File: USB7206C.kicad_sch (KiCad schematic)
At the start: 38 parts, among them J1 USB_SPI_(Opt), SW1 RESET_HUB, U2 MIC803-29D4VM3-TR, U27 USB7206C/KDX, Y1 25MHz

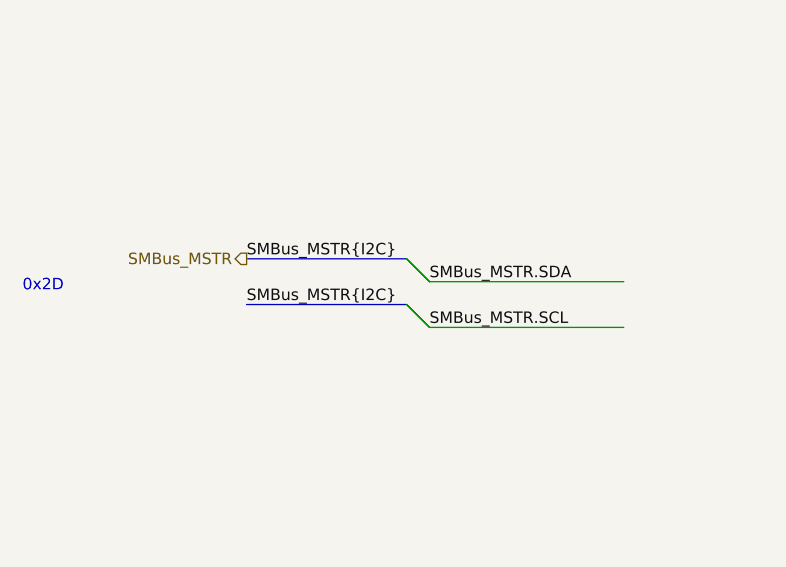
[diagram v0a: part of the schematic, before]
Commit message: Ferrite Breads added for 5V, TVS and ESD diodes added
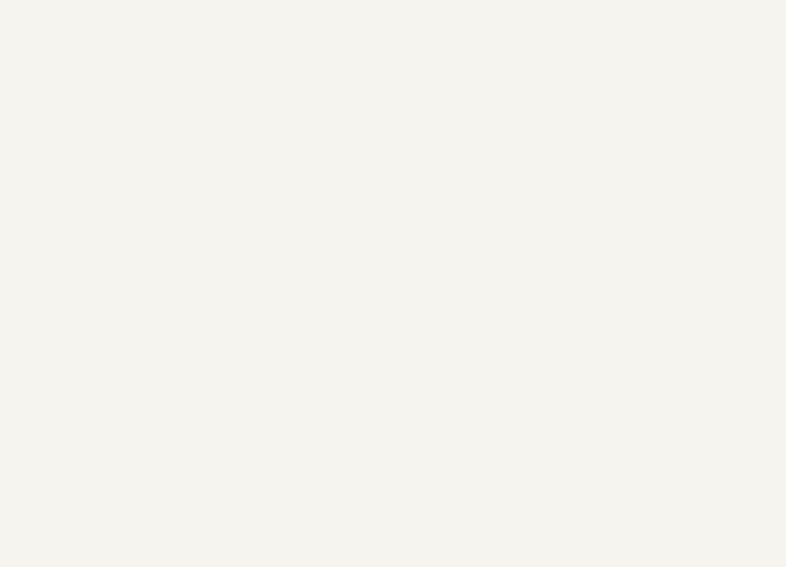
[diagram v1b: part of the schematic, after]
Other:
- note removed: "0x2D"
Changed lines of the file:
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@@
 		)
 	)
-	(text "0x2D"
-		(exclude_from_sim no)
-		(at -93.726 77.978 0)
-		(effects
-			(font
-				(size 1.27 1.27)
-			)
-		)
-	)
 	(text "VBUS Detection & ESD Protection"
 		(exclude_from_sim no)
@@
 	)
 	(bus_entry
-		(at -53.34 80.01)
-		(size 2.54 2.54)
-		(stroke
-			(width 0)
-			(type default)
-		)
-	)
-	(bus_entry
 		(at 191.77 26.67)
 		(size -2.54 2.54)
@@
 	)
 	(bus_entry
-		(at -53.34 74.93)
-		(size 2.54 2.54)
-		(stroke
-			(width 0)
-			(type default)
-		)
-	)
-	(bus_entry
 		(at 191.77 138.43)
 		(size -2.54 2.54)
@@
 	)
 	(bus_entry
-		(at -50.8 77.47)
-		(size -2.54 -2.54)
-		(stroke
-			(width 0)
-			(type default)
-		)
-	)
-	(bus_entry
 		(at 41.91 34.29)
 		(size 2.54 2.54)
@@
 	)
 	(bus_entry
-		(at -50.8 82.55)
-		(size -2.54 -2.54)
-		(stroke
-			(width 0)
-			(type default)
-		)
-	)
-	(bus_entry
 		(at 191.77 113.03)
 		(size -2.54 2.54)
@@
 	(wire
 		(pts
-			(xy -50.8 77.47) (xy -29.21 77.47)
-		)
-		(stroke
-			(width 0)
-			(type default)
-		)
-	)
-	(wire
-		(pts
 			(xy 44.45 41.91) (xy 60.96 41.91)
 		)
@@
 	(wire
 		(pts
-			(xy -50.8 82.55) (xy -29.21 82.55)
-		)
-		(stroke
-			(width 0)
-			(type default)
-		)
-	)
-	(wire
-		(pts
 			(xy 234.95 40.64) (xy 251.46 40.64)
 		)
@@
 		)
 	)
-	(bus
-		(pts
-			(xy -71.12 80.01) (xy -53.34 80.01)
-		)
-		(stroke
-			(width 0)
-			(type default)
-		)
-	)
 	(wire
 		(pts
@@
 		)
 	)
-	(bus
-		(pts
-			(xy -71.12 74.93) (xy -53.34 74.93)
-		)
-		(stroke
-			(width 0)
-			(type default)
-		)
-	)
 	(wire
 		(pts
@@
 		)
 	)
-	(label "SMBus_MSTR{I2C}"
-		(at -71.12 74.93 0)
-		(effects
-			(font
-				(size 1.27 1.27)
-			)
-			(justify left bottom)
-		)
-	)
 	(label "USB3_DN5.TX1-"
 		(at 172.72 137.16 0)
@@
 		)
 	)
-	(label "SMBus_MSTR.SDA"
-		(at -50.8 77.47 0)
-		(effects
-			(font
-				(size 1.27 1.27)
-			)
-			(justify left bottom)
-		)
-	)
 	(label "USB3_DN3.RX1+"
 		(at 172.72 90.17 0)
@@
 		)
 	)
-	(label "SMBus_MSTR.SCL"
-		(at -50.8 82.55 0)
-		(effects
-			(font
-				(size 1.27 1.27)
-			)
-			(justify left bottom)
-		)
-	)
 	(label "CFG_STRAP1"
 		(at 30.48 259.08 0)
@@
 		)
 	)
-	(label "SMBus_MSTR{I2C}"
-		(at -71.12 80.01 0)
-		(effects
-			(font
-				(size 1.27 1.27)
-			)
-			(justify left bottom)
-		)
-	)
 	(label "USB3_UP.RX1+"
 		(at 60.96 41.91 180)
@@
 		)
 	)
-	(hierarchical_label "SMBus_MSTR"
-		(shape output)
-		(at -71.12 74.93 180)
-		(effects
-			(font
-				(size 1.27 1.27)
-			)
-			(justify right)
-		)
-	)

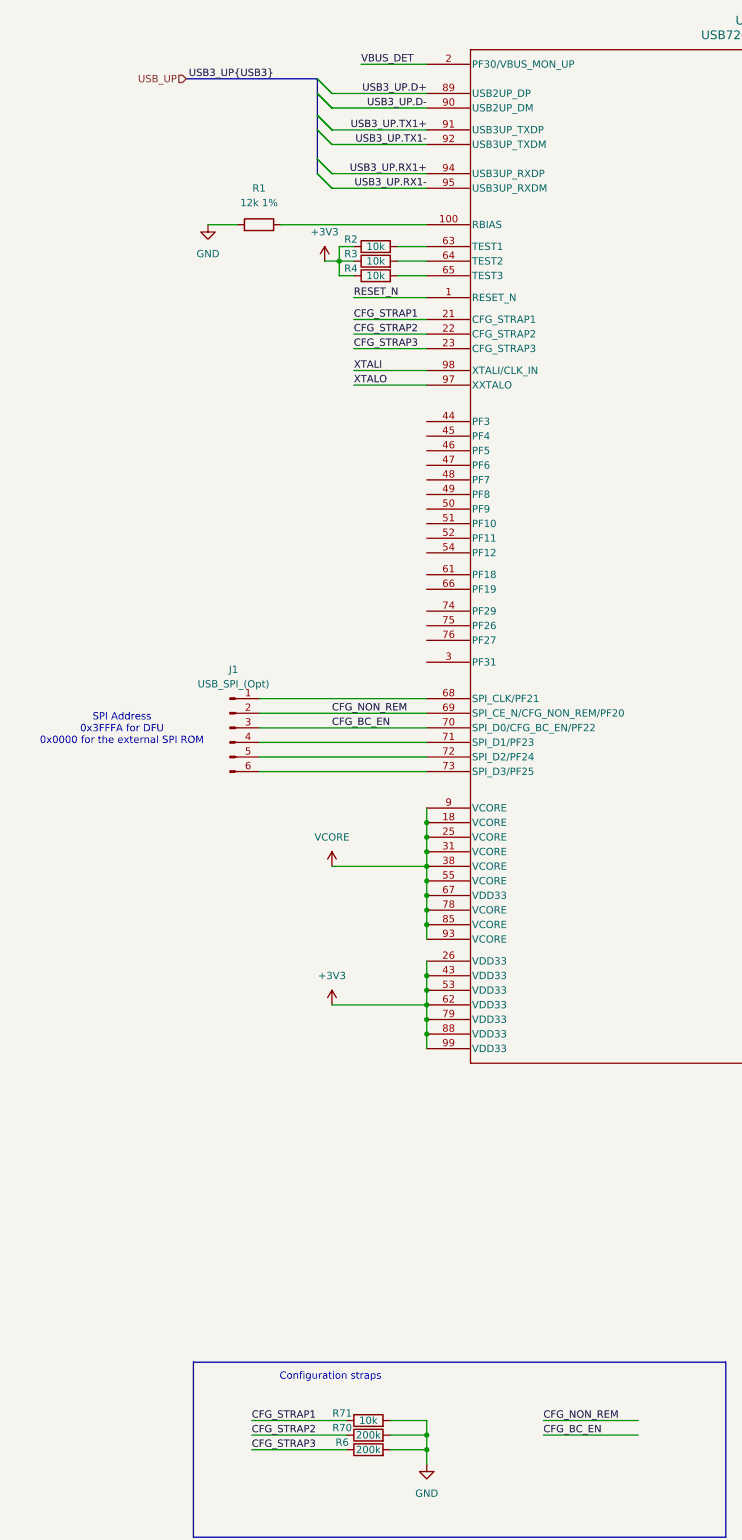
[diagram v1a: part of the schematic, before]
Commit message: Ferrite bread filter for LDO and MIC23201, labelling improved
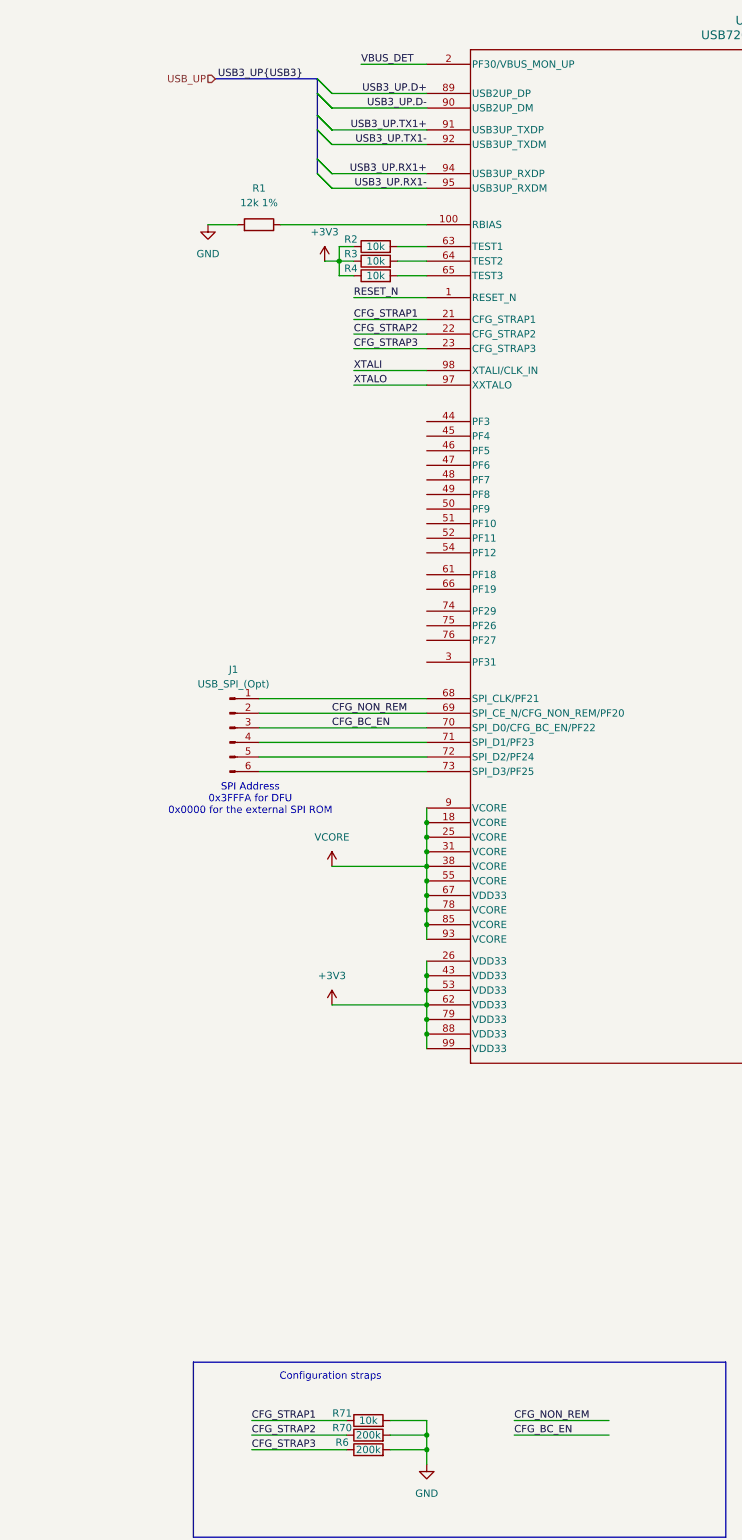
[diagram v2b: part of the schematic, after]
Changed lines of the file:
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@@
 	(text "SPI Address\n0x3FFFA for DFU\n0x0000 for the external SPI ROM"
 		(exclude_from_sim no)
-		(at 7.874 138.684 0)
+		(at 30.226 150.876 0)
 		(effects
 			(font
@@
 	(bus
 		(pts
-			(xy 19.05 25.4) (xy 41.91 25.4)
+			(xy 24.13 25.4) (xy 41.91 25.4)
 		)
 		(stroke
@@
 	(wire
 		(pts
-			(xy 81.28 261.62) (xy 97.79 261.62)
+			(xy 76.2 261.62) (xy 92.71 261.62)
 		)
 		(stroke
@@
 	(wire
 		(pts
-			(xy 81.28 259.08) (xy 97.79 259.08)
+			(xy 76.2 259.08) (xy 92.71 259.08)
 		)
 		(stroke
@@
 	)
 	(label "CFG_BC_EN"
-		(at 81.28 261.62 0)
+		(at 76.2 261.62 0)
 		(effects
 			(font
@@
 	)
 	(label "CFG_NON_REM"
-		(at 81.28 259.08 0)
+		(at 76.2 259.08 0)
 		(effects
 			(font
@@
 	)
 	(label "USB3_UP{USB3}"
-		(at 34.29 25.4 180)
+		(at 39.37 25.4 180)
 		(effects
 			(font
@@
 	(hierarchical_label "USB_UP"
 		(shape input)
-		(at 19.05 25.4 180)
+		(at 24.13 25.4 180)
 		(effects
 			(font
